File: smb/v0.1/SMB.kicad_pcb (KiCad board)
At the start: 2 copper layers, 100 x 86 mm, 98 parts, among them IC1 MAX485, IC101 ATMEGA1284-A, IC2 DS2482-100S, J101 RJ45, J102 RTS_RESET, J103 ICSP, J104 SERIAL_REV, J202 USD_CONN, J401 HR911105_RJ45, P1 CONN_2, P101 I2C_CONN, P102 CONN_10X2, P103 CONN_3X2, P105 CONN_5, P107 CONN_3, P108 CONN_5, P109 CONN_3, P110 CONN_3, P2 CONN_3, P301 CONN_2, SW101 SKQGAKE010, U201 ENC28J60, U202 LM1117IMP-3.3, U301 74HC08, U302 MP2562DS, U303 74HC08, X101 20MHz, X201 25MHz

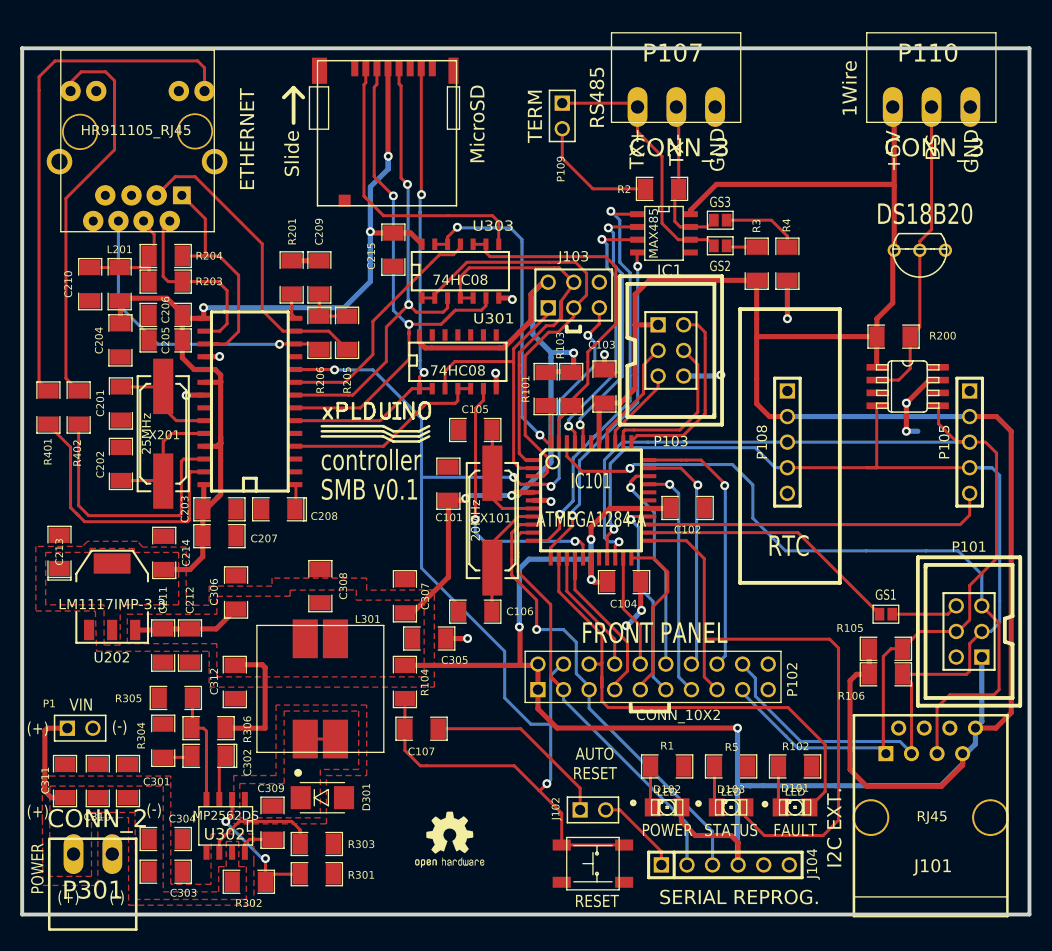
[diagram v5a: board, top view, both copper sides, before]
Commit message: creation d'un support type "shield" pour permettre de personnaliser le circuit mis en place d'un mini connecteur 2 points reli?s au shield serigraphie
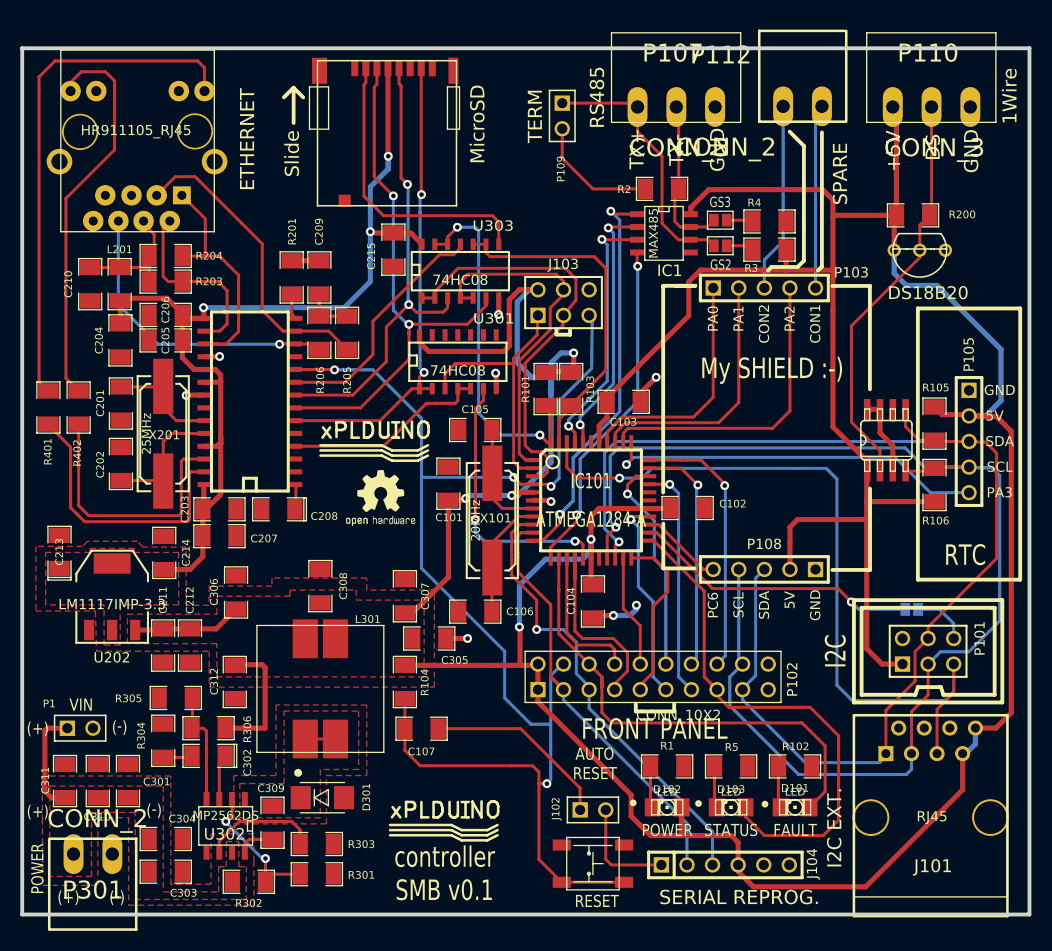
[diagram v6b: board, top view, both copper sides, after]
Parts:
- removed the logo_xplduino at (68.1, 64.8)
- added P112: CONN_2, MOL_CONN_2_MINI, F.Cu at (110.5, 32.8)
- added logo_xplduino: VAL**, logo_xplduino, F.Cu at (74.9, 104.4)
- added logo_xplduino: VAL**, logo_xplduino, F.Cu at (67.9, 66.7)
- GS1: moved to B.Cu
- P103: value CONN_3X2 -> CONN_5; footprint HE10-6 -> PIN_ARRAY_5x1
- moved G*** 34.6 mm to (64.8, 67.9)
- moved R105 22.9 mm to (123.6, 64.3), turned to 270 degrees
- moved R106 19.4 mm to (123.6, 70.4), turned to 90 degrees
- moved P108 12.8 mm to (106.7, 78.7), turned to 180 degrees
- moved R200 12.2 mm to (121.4, 43.6)
- moved P103 11.2 mm to (106.7, 50.8), turned to 0 degrees
- moved IC2 5.74 mm to (118.8, 65.9), turned to 0 degrees
- moved R4 4.55 mm to (107.2, 44.2), turned to 0 degrees
- moved P101 4.52 mm to (122.9, 86.9), turned to 0 degrees
- moved C104 3.63 mm to (89.7, 81.9), turned to 90 degrees
- moved GS1 2.61 mm to (121.3, 82.7), turned to 90 degrees
- moved C103 2.44 mm to (92.7, 62.1), turned to 0 degrees
- moved R3 1.89 mm to (107.2, 47.0), turned to 0 degrees
- moved J103 1.26 mm to (86.7, 52.2)
- moved P105 0.09 mm to (127.0, 66.0)
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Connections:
- P103 pad 1: +5V -> PA0
- P103 pad 2: PA3 -> PA1
- P103 pad 3: PA0 -> N-0000029
- P103 pad 5: PA1 -> N-0000028
- P105 pad 5: PC6 -> PA3
- P108 pad 5: DS -> PC6
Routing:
- net PC6: track 34.4 -> 8.26 mm
- net PA3: track 19.1 -> 38.1 mm, vias 0 -> 1
- net N-0000029: track 0.00 -> 18.8 mm
- net N-0000028: track 0.00 -> 18.3 mm
- net PA1: track 8.39 -> 25.9 mm
- net PA2: track 16.0 -> 30.6 mm
- net SDA: track 111.9 -> 125.9 mm
- net PA0: track 11.3 -> 23.8 mm
- net SCL: track 117.2 -> 128.8 mm
- net N-0000030: track 30.7 -> 40.6 mm
- net LED_FAULT: track 62.2 -> 54.0 mm
- net +5V: track 420.3 -> 426.7 mm, vias 7 -> 5
- net GND: track 35.2 -> 29.3 mm, vias 13 -> 9
- net N-0000013: track 7.77 -> 2.66 mm
- net RX1: track 43.6 -> 47.5 mm
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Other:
- board text added: "5V"
- board text added: "CON1"
- board text added: "CON2"
- board text added: "I2C"
- board text added: "My SHIELD :-)"
- board text added: "PA0"
- board text added: "PA1"
- board text added: "PA2"
- board text added: "PA3"
- board text added: "PC6"
- board text added: "SCL"
- board text added: "SDA"
- board text added: "SPARE"

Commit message: Modification Routage SMB :         Connecteur Spare 3 broches avec GND         RX1 et TX1 sans via         Suppression via sur connexion vers front panel         Changement de place des nom pour le connecteur My Shield (Haut)         Modification du cable reset
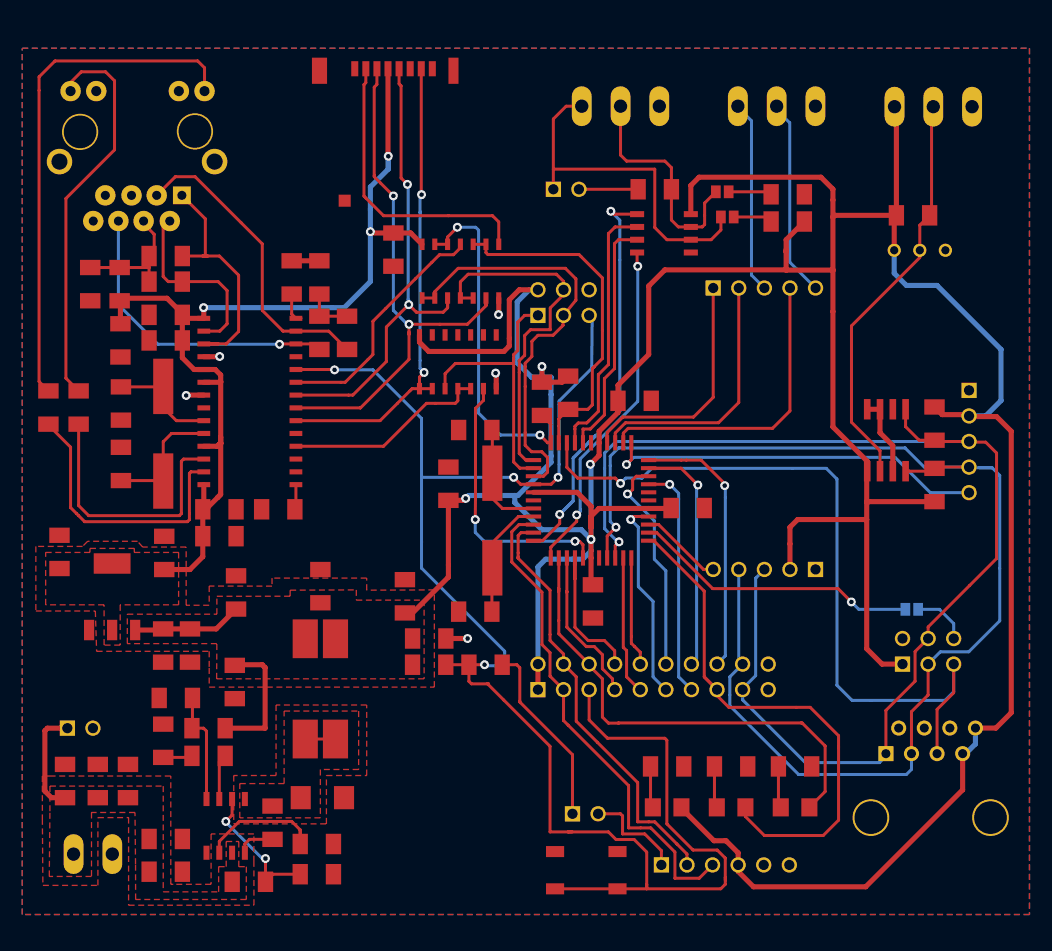
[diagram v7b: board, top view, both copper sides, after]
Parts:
- removed the logo_xplduino at (74.9, 104.4)
- removed the logo_xplduino at (67.9, 66.7)
- added logo_xplduino: VAL**, logo_xplduino, F.Cu at (75.0, 103.8)
- P112: value CONN_2 -> CONN_3; footprint MOL_CONN_2_MINI -> MOL_CONN_3_MINI
- moved C107 8.99 mm to (79.0, 88.2)
- moved P109 7.29 mm to (87.0, 41.0), turned to 0 degrees
- moved P107 5.54 mm to (96.2, 32.8)
- moved R3 3.33 mm to (109.0, 44.2)
- moved R4 3.25 mm to (109.0, 41.5)
- moved R104 2.96 mm to (73.4, 88.2), turned to 0 degrees
- moved GS2 2.94 mm to (103.0, 43.8)
- moved GS3 2.83 mm to (102.5, 41.2)
- moved P112 1.26 mm to (111.8, 32.8)
- moved C103 1.09 mm to (93.8, 62.0)
- moved R101 1.03 mm to (84.6, 61.8)
- moved SW101 0.93 mm to (89.0, 108.6)
- moved J102 0.85 mm to (88.9, 103.0)
- moved R2 0.72 mm to (95.8, 41.0)
- moved G*** 0.66 mm to (64.4, 67.4)
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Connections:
- IC1 pad 2: PB0 -> PB1
- IC1 pad 3: PB1 -> PB0
- IC101 pad 29: N-0000012 -> (no net)
- IC2 pad 6: N-0000023 -> (no net)
- J202 pad 1: N-0000087 -> (no net)
- J202 pad 8: N-0000088 -> (no net)
- J401 pad 5: N-0000058 -> (no net)
- P102 pad 10: PC2 -> PC3
- P102 pad 3: TX0 -> RX0
- P102 pad 4: /RESET -> TX0
- P102 pad 5: RX0 -> /RESET
- P102 pad 7: PD6 -> PD5
- P102 pad 8: PD5 -> PD6
- P102 pad 9: PC3 -> PC2
- P103 pad 3: N-0000029 -> N-0000030
- P103 pad 5: N-0000028 (its old number) -> N-0000031
- P112 pad 1: N-0000028 (its old number) -> GND
- P112 pad 2: N-0000029 -> N-0000031
- U201 pad 3: N-0000072 -> (no net)
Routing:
- net /RESET: track 134.3 -> 163.2 mm
- net N-0000031: track 0.00 -> 19.6 mm
- net N-0000030: track 0.00 -> 19.1 mm
- net N-0000029: track 18.8 -> 0.00 mm
- net N-0000028 (its old number): track 18.3 -> 0.00 mm
- net GND: track 29.3 -> 19.4 mm, vias 9 -> 5
- net +5V: track 426.7 -> 417.4 mm, vias 5 -> 4
- net TX+: track 26.4 -> 34.9 mm
- net TX-: track 16.0 -> 23.0 mm
- net N-0000021: track 12.4 -> 5.88 mm
- net PD6: track 21.7 -> 15.2 mm
- net PC3: track 17.0 -> 10.9 mm
- net RX0: track 45.3 -> 49.1 mm, vias 1 -> 0
- net TX0: track 44.9 -> 42.5 mm
- net PB0: track 26.1 -> 23.9 mm, vias 2 -> 0
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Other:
- board outline removed
- board text added: "1WIRE"
- board text removed: "1Wire"
